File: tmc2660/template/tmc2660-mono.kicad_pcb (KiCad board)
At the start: 4 copper layers, 25 x 40 mm, 18 parts, among them J100 0R, M100 Mount, M101 Mount, P100 Motor, U100 TMC2660

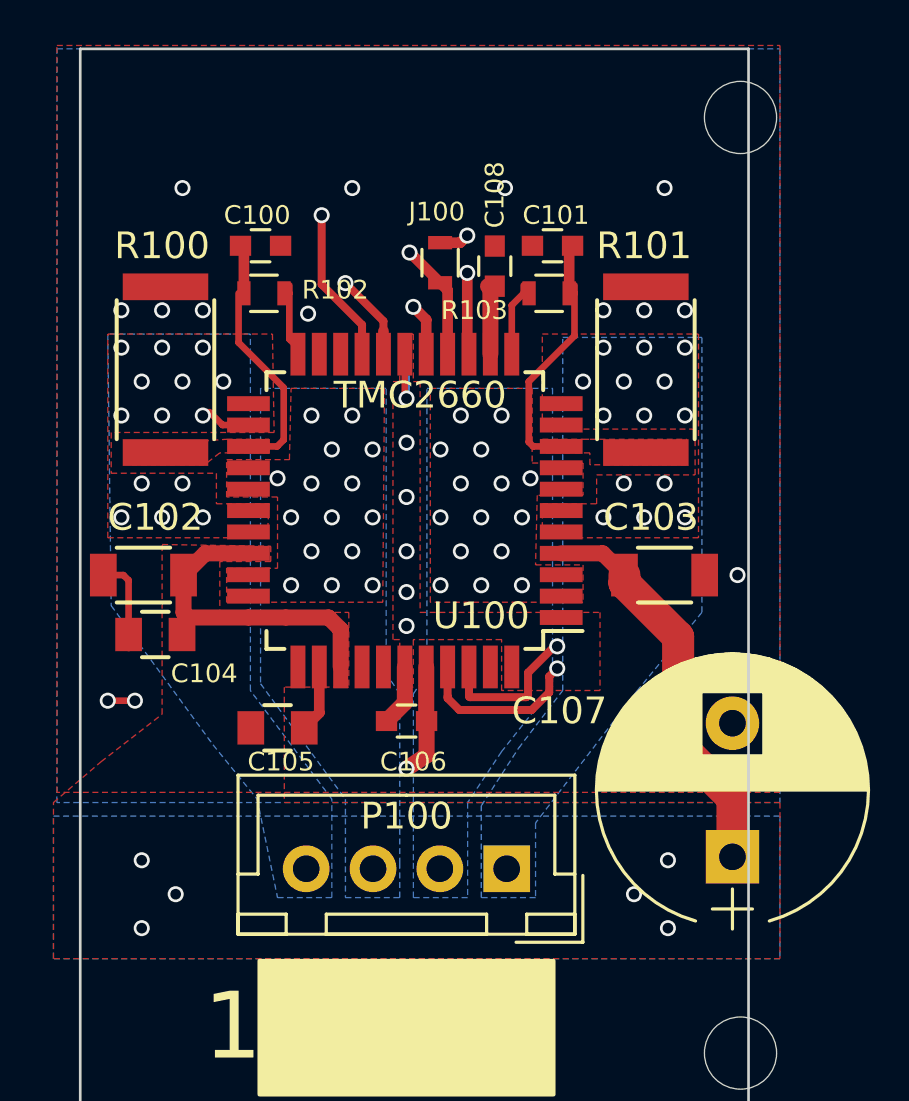
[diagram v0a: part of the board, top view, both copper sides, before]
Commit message: Template: make work with larger annular ring sizes.
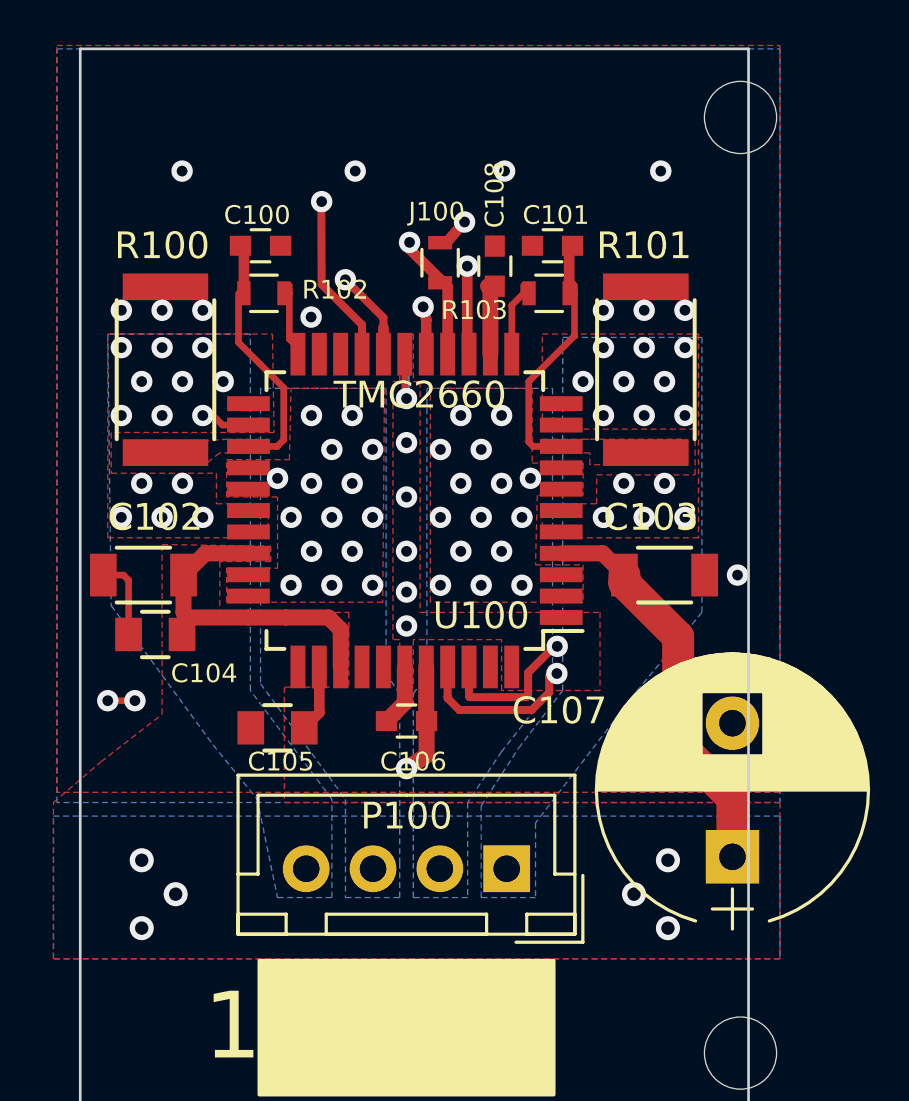
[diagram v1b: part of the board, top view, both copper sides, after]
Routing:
- net /TMC2660-100/~EN: track 30.8 -> 31.3 mm
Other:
- net class Default: via_dia 0.6 -> 0.8
- net class MotPower: via_dia 0.6 -> 0.9; via_drill 0.4 -> 0.5
- rule via_min_drill: 0.3 -> 0.4
- rule via_min_size: 0.4 -> 0.7

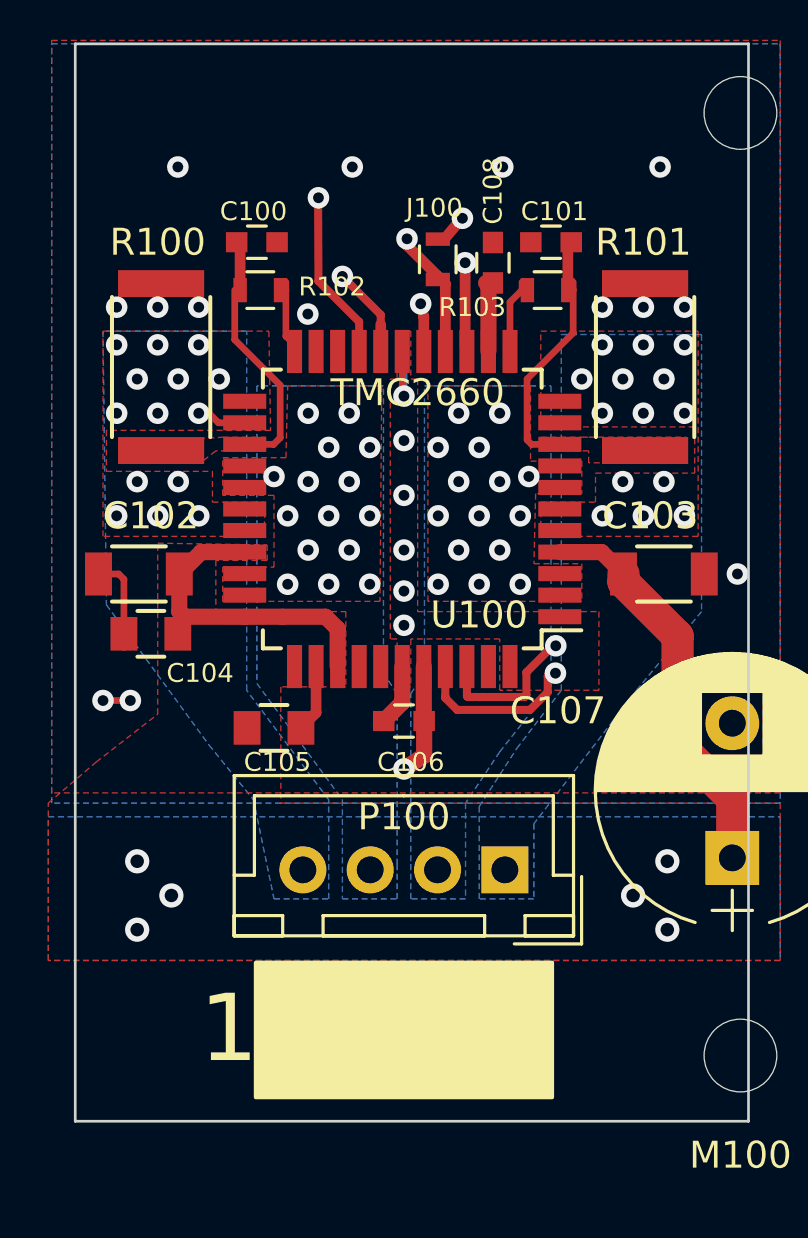
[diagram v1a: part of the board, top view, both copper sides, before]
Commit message: Make some copper areas flow better.
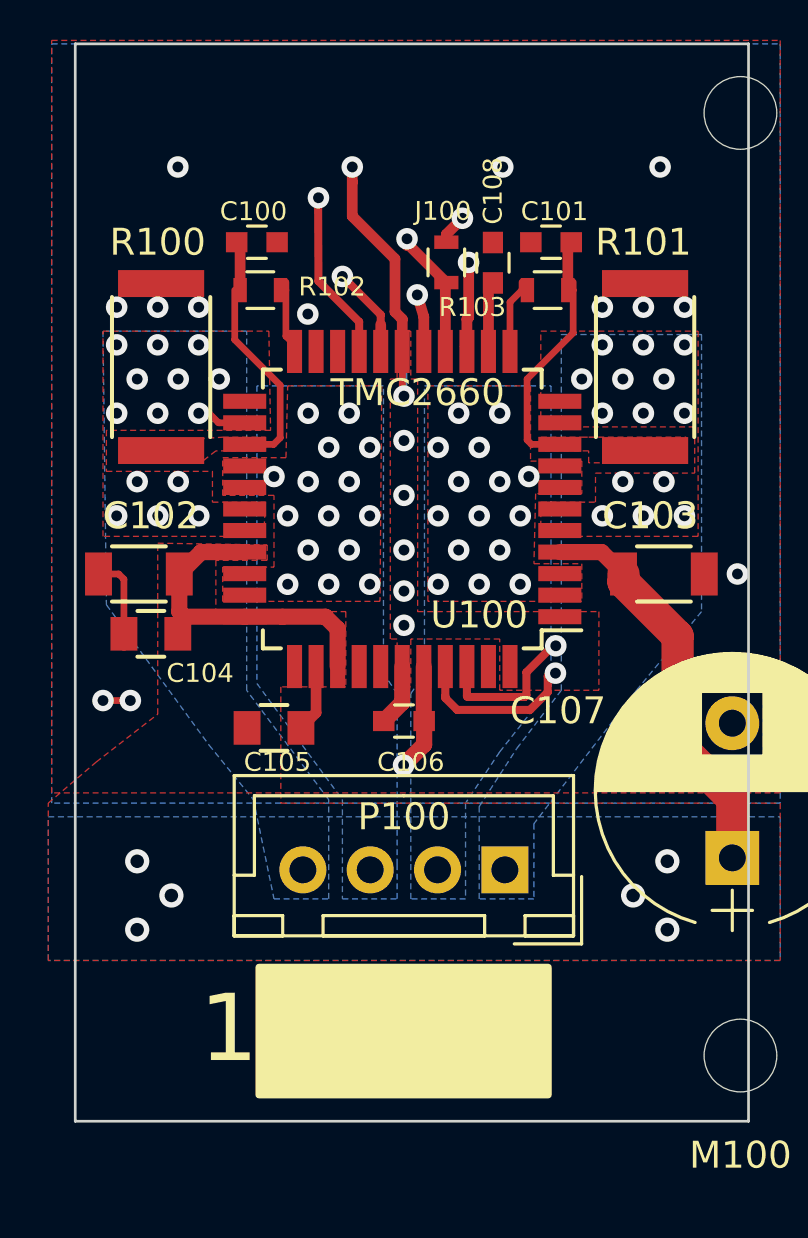
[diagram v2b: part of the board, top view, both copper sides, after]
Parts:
- moved J100 0.34 mm to (85.4, 56.6)
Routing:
- net GND: track 9.82 -> 17.4 mm
- net /TMC2660-100/MISO: track 17.9 -> 18.4 mm
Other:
- rule via_min_size: 0.7 -> 0.8

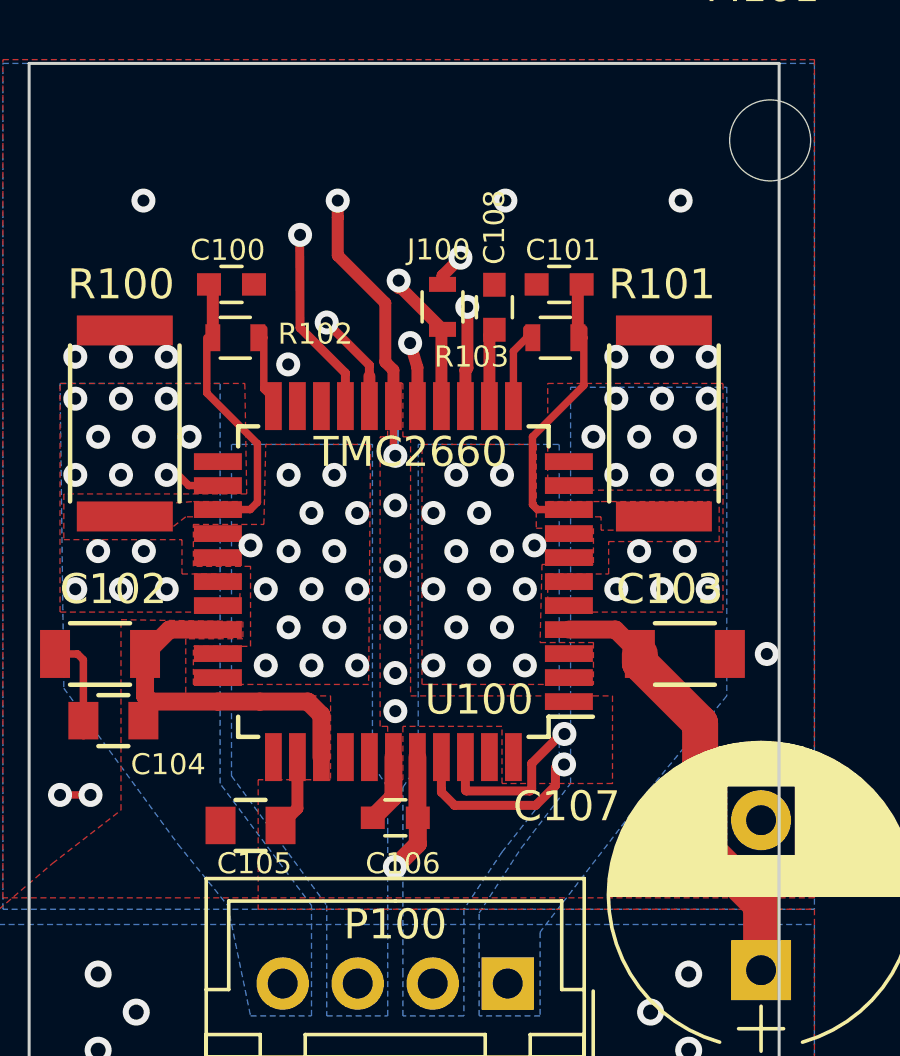
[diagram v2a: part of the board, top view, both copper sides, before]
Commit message: Manufacturability: some board houses want 0.2mm/8mil structure size for 70um/2oz copper.
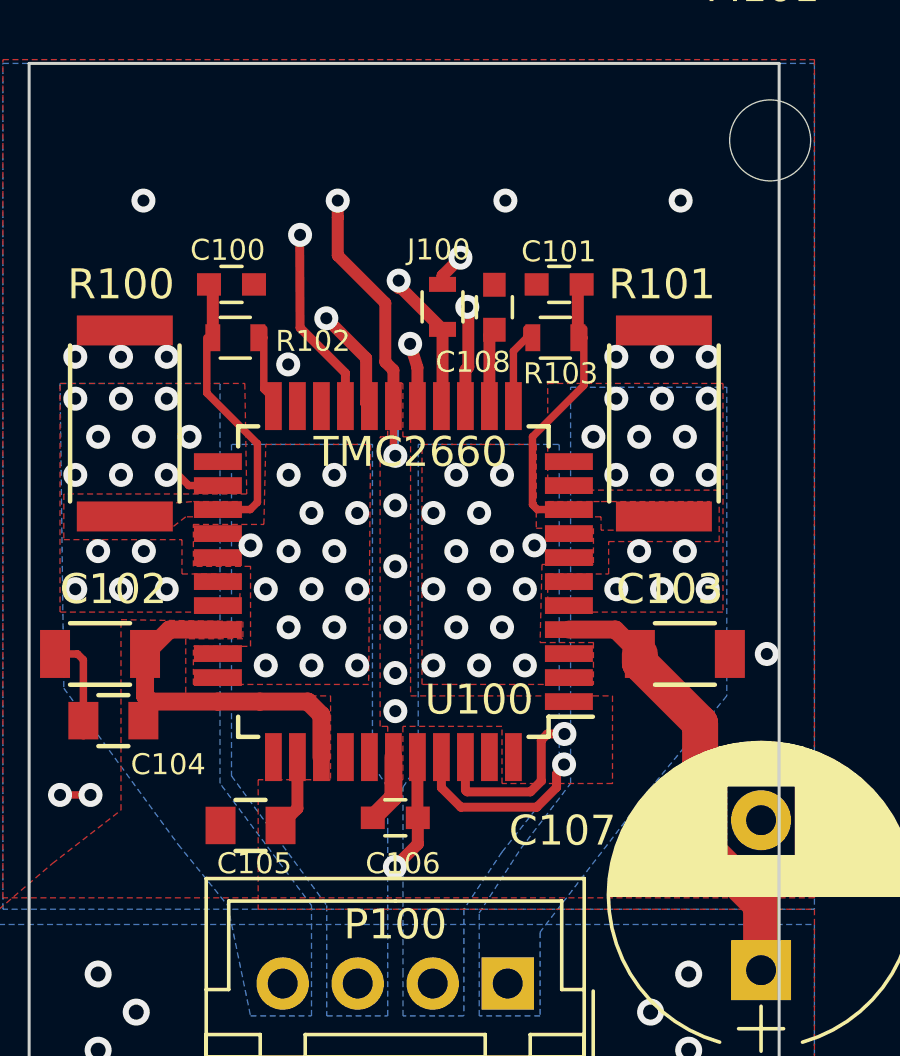
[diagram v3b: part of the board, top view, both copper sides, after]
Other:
- net class Default: clearance 0.18 -> 0.21
- rule trace_clearance: 0.18 -> 0.21

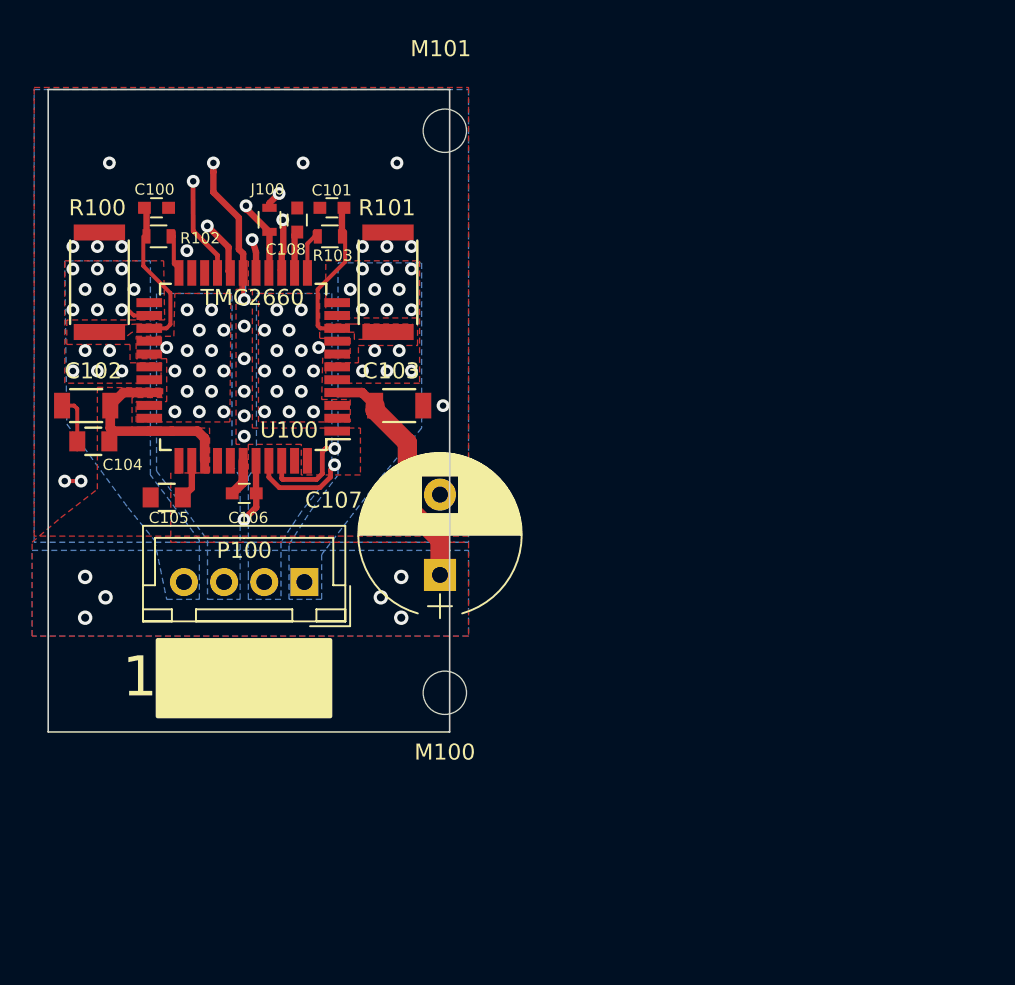
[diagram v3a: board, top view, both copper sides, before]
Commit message: Move template to a somewhat sane (100,100) origin.
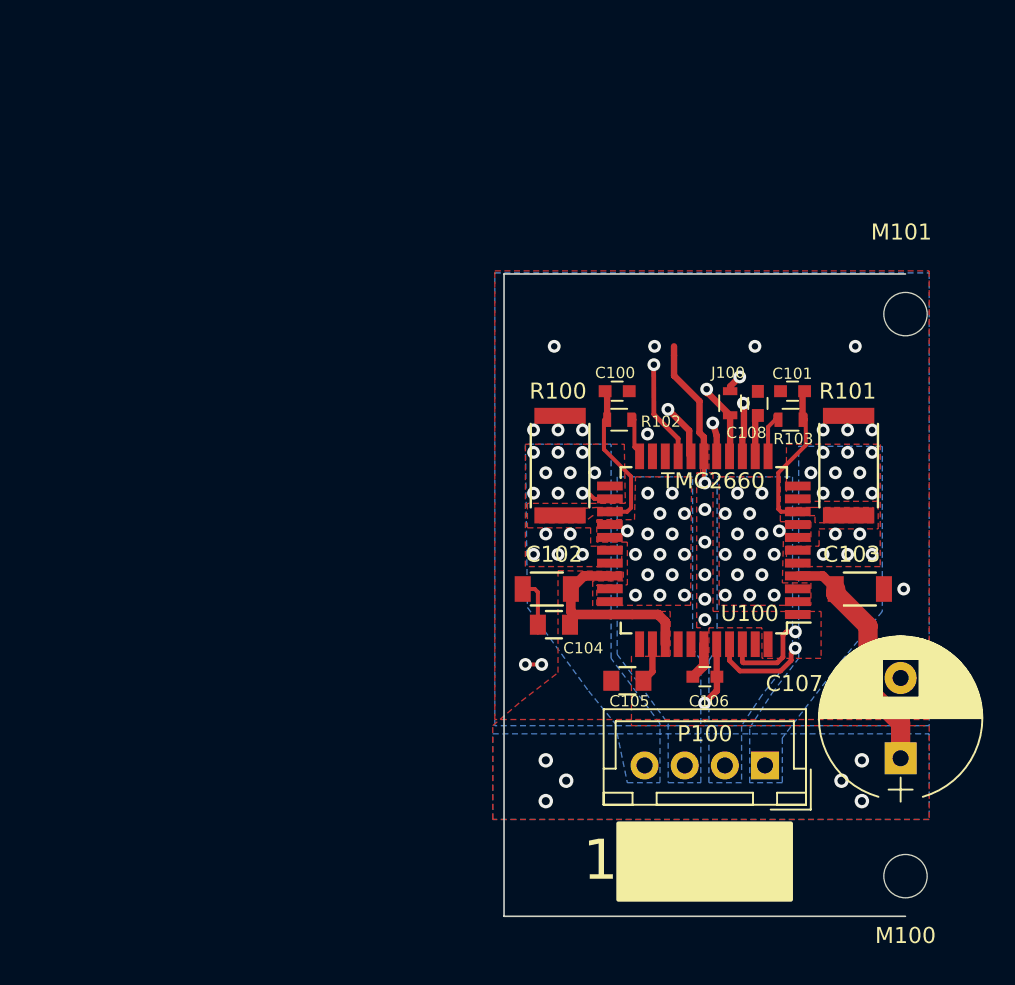
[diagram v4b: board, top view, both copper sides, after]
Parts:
- moved C103 30.9 mm to (122.2, 79.6)
- moved C104 30.9 mm to (103.1, 81.8)
- moved C105 30.9 mm to (107.7, 85.3)
- moved C106 30.9 mm to (112.5, 85.1)
- moved M100 30.9 mm to (125.0, 97.5)
- moved M101 30.9 mm to (125.0, 62.5)
- moved R100 30.9 mm to (103.5, 71.9)
- moved R101 30.9 mm to (121.5, 71.9)
- moved R103 30.9 mm to (117.8, 69.1)
- moved C100 30.9 mm to (107.0, 67.3)
- moved C108 30.9 mm to (115.8, 68.1)
- moved C101 30.9 mm to (118.0, 67.3)
- moved C102 30.9 mm to (102.7, 79.6)
- moved C107 30.9 mm to (124.7, 90.2)
- moved J100 30.9 mm to (114.1, 68.0)
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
